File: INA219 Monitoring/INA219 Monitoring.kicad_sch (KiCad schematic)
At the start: 7 parts, among them U1 INA219AxDCN

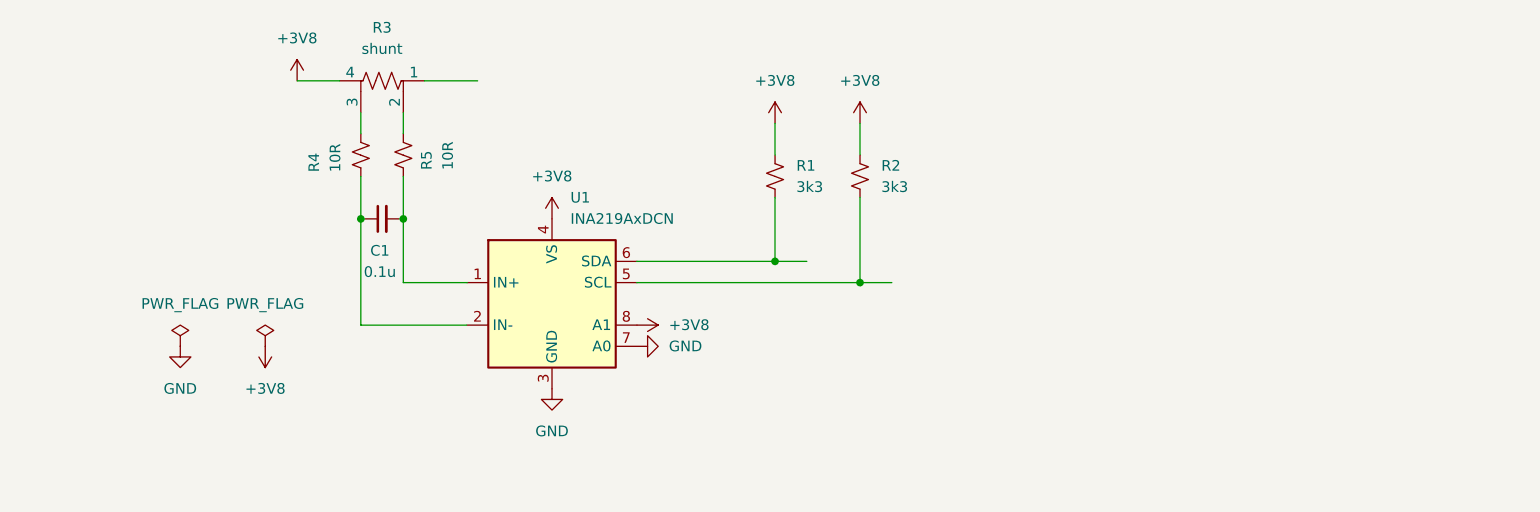
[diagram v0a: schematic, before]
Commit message: Started 3V3 and 5V out
Started working in the 3V3 and 5V output module and assigned footprints to the INA219 module
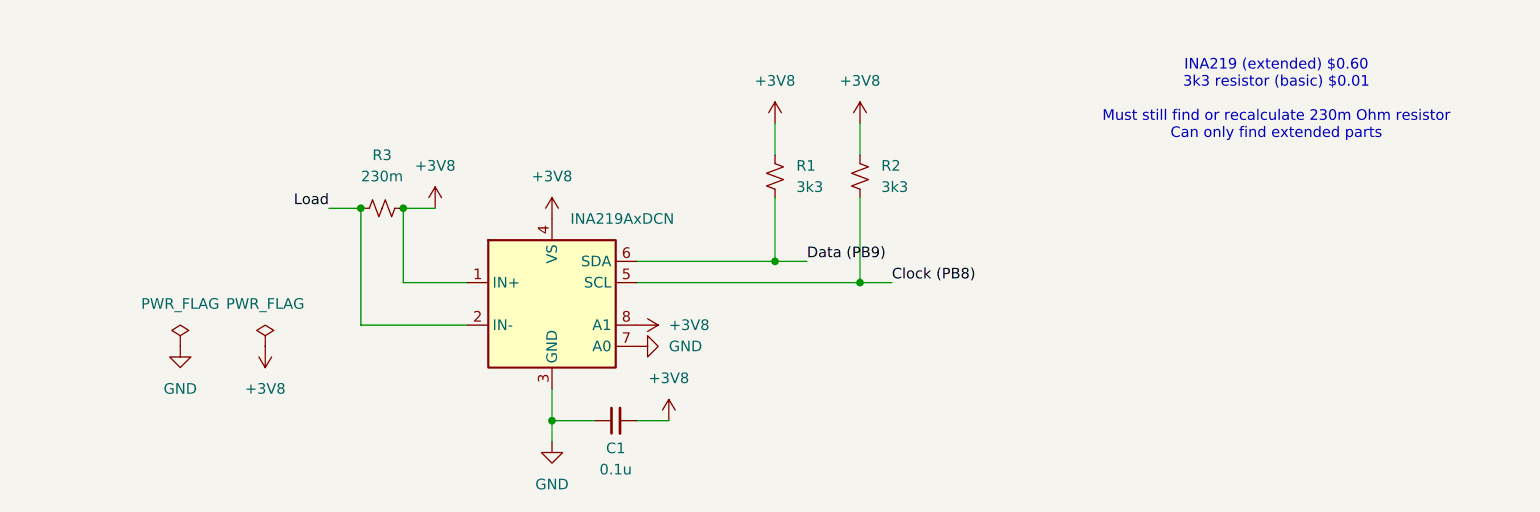
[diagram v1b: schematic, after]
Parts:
- removed R3: shunt, symbol Device:R_Shunt_US
- removed R4, R5: 10R, symbol Device:R_Small_US
- added R3: 230m, symbol Device:R_Small_US
- C1: LCSC (none) -> C14663
- R1, R2: LCSC (none) -> C22978
- U1: LCSC (none) -> C87469
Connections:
- net +3V8: now also C1.2, U1.1 (IN+), R3.2
- net GND: now also C1.1
- net Clock (PB8): now reaches R2.2, U1.5 (SCL)
- net Load: now reaches U1.2 (IN-)
- net Load: now also R3.1; no longer C1.1
- net Data (PB9): now reaches R1.2, U1.6 (SDA)
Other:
- note added: "INA219 (extended) $0.60 3k3 resistor (basic) $0.01 Must still find or recalculate 230m Ohm resistor Can only find extended parts"

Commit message: Added bidirectional motor control section
Completed the bidirectional motor control part of the system as well as finished the remaining part of the 3V3 and 5V out.
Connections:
- net +3V8: no longer C1.2, R1.1, R2.1, R3.2, U1.1 (IN+), U1.4 (VS), U1.8 (A1)
- new net +3V3: R1.1, R2.1, U1.4 (VS), U1.8 (A1)
- new net +3V7: C1.2, R3.2, U1.1 (IN+)
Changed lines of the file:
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@@
 		(on_board yes)
 		(dnp no)
-		(fields_autoplaced yes)
 		(property "Reference" "#PWR07"
 			(at 170.18 115.57 0)
@@
 			)
 		)
-		(property "Value" "+3V8"
-			(at 170.18 106.68 0)
-			(effects
-				(font
-					(size 1.27 1.27)
-				)
+		(property "Value" "+3V3"
+			(at 170.942 108.712 0)
+			(effects
+				(font
+					(size 1.27 1.27)
+				)
+				(justify left)
 			)
 		)
@@
 		(on_board yes)
 		(dnp no)
-		(fields_autoplaced yes)
 		(property "Reference" "#PWR06"
 			(at 207.01 104.14 0)
@@
 			)
 		)
-		(property "Value" "+3V8"
-			(at 207.01 95.25 0)
-			(effects
-				(font
-					(size 1.27 1.27)
-				)
+		(property "Value" "+3V3"
+			(at 204.724 96.012 0)
+			(effects
+				(font
+					(size 1.27 1.27)
+				)
+				(justify left)
 			)
 		)
@@
 			)
 		)
-		(property "Value" "+3V8"
-			(at 156.21 105.41 0)
-			(effects
-				(font
-					(size 1.27 1.27)
-				)
+		(property "Value" "+3V7"
+			(at 158.75 109.2199 0)
+			(effects
+				(font
+					(size 1.27 1.27)
+				)
+				(justify left)
 			)
 		)
@@
 			)
 		)
-		(property "Value" "+3V8"
+		(property "Value" "+3V3"
 			(at 184.15 124.4599 90)
 			(effects
@@
 			)
 		)
-		(property "Value" "+3V8"
-			(at 184.15 130.81 0)
-			(effects
-				(font
-					(size 1.27 1.27)
-				)
+		(property "Value" "+3V7"
+			(at 186.69 134.6199 0)
+			(effects
+				(font
+					(size 1.27 1.27)
+				)
+				(justify left)
 			)
 		)
@@
 		(on_board yes)
 		(dnp no)
-		(fields_autoplaced yes)
 		(property "Reference" "#PWR05"
 			(at 196.85 104.14 0)
@@
 			)
 		)
-		(property "Value" "+3V8"
-			(at 196.85 95.25 0)
-			(effects
-				(font
-					(size 1.27 1.27)
-				)
-			)
-		)
+		(property "Value" "+3V3"
+			(at 194.31 96.266 0)
+			(effects
+				(font
+					(size 1.27 1.27)
+				)
+				(justify left)
+			)
+		)

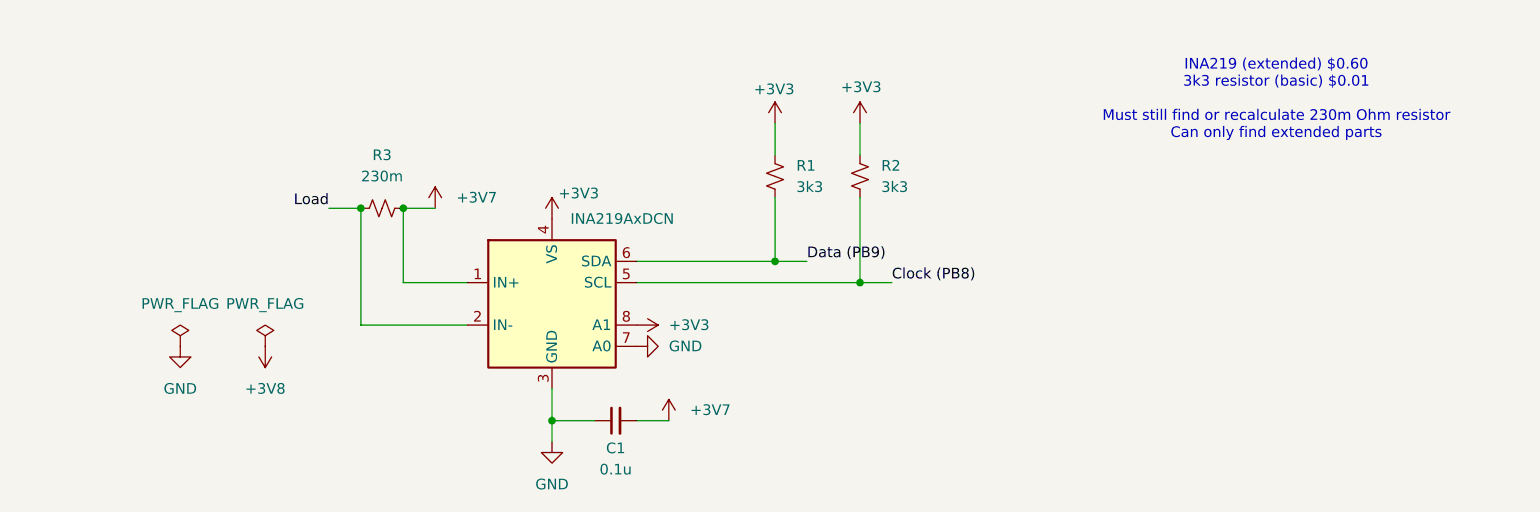
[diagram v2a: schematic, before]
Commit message: ON/OFF switch
Completed the ON/OFF switch.
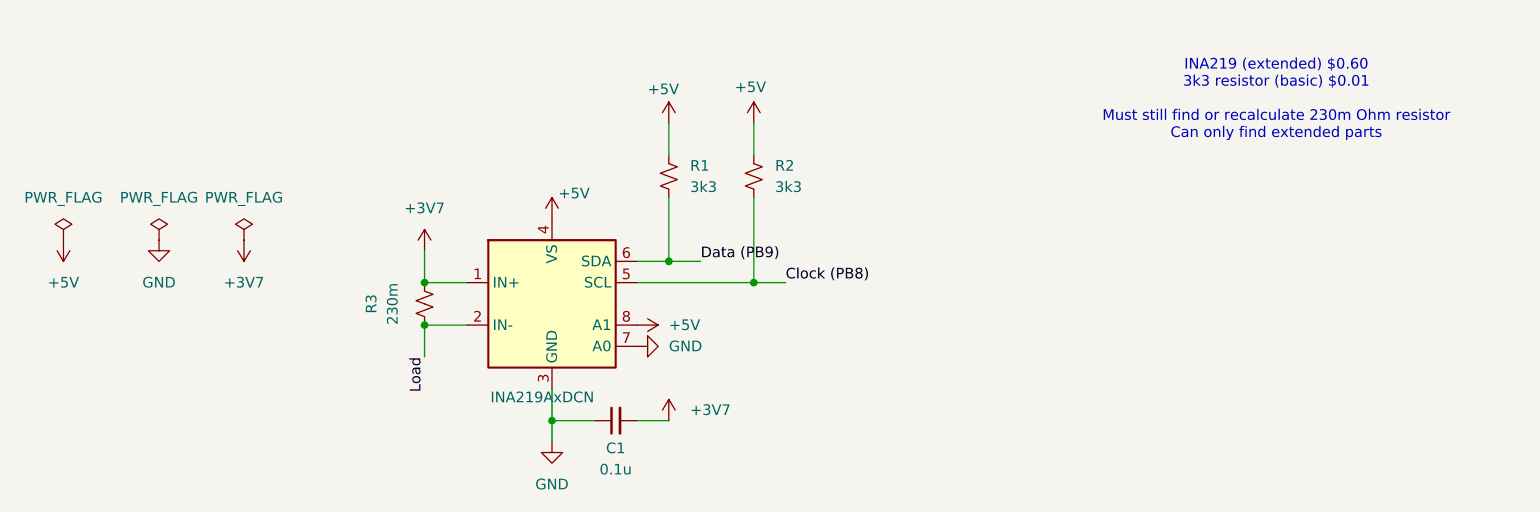
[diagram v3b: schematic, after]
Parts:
- C1: footprint (none) -> Capacitor_SMD:C_0603_1608Metric_Pad1.08x0.95mm_HandSolder
- R1, R2: footprint (none) -> Resistor_SMD:R_0603_1608Metric_Pad0.98x0.95mm_HandSolder
- R3: footprint (none) -> Resistor_SMD:R_1206_3216Metric_Pad1.30x1.75mm_HandSolder; LSCS (none) -> C25336
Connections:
- net +3V3 renamed +5V
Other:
- moved on the sheet: R1, R2, R3
